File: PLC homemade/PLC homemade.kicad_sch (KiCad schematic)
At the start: 18 parts, among them J14 Conn_01x02, J15 Conn_01x02, U1 XC6220B331MR, U2 XL1509-5.0E1

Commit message: :ambulance:2output and usbc
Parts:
- J15: footprint Connector_PinHeader_1.00mm:PinHeader_1x02_P1.00mm_Vertical_SMD_Pin1Left -> PhoenixContact_GMSTBA_2,5_2-G_1x02_P7.50mm_Horizontal
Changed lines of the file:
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@@
 			)
 		)
-		(property "Footprint" "Connector_PinHeader_1.00mm:PinHeader_1x02_P1.00mm_Vertical_SMD_Pin1Left"
+		(property "Footprint" "PhoenixContact_GMSTBA_2,5_2-G_1x02_P7.50mm_Horizontal"
 			(at 105.41 72.39 0)
 			(effects

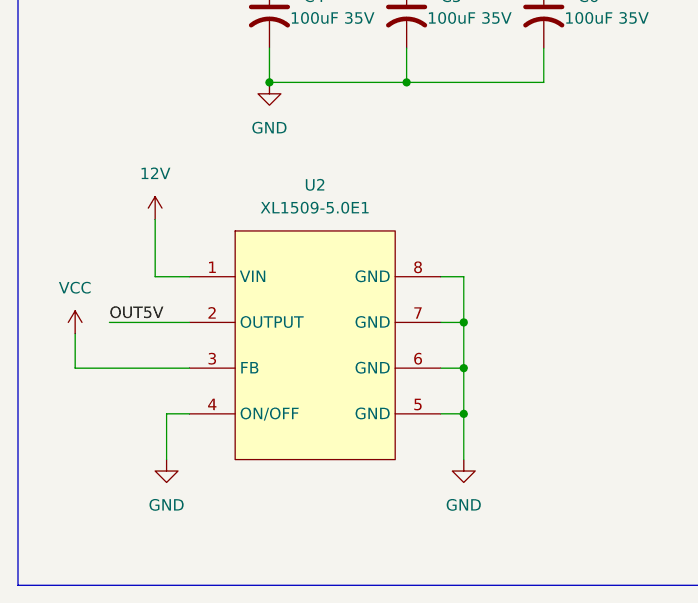
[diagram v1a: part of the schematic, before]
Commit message: :ambulance: Changed the 5 footprint error
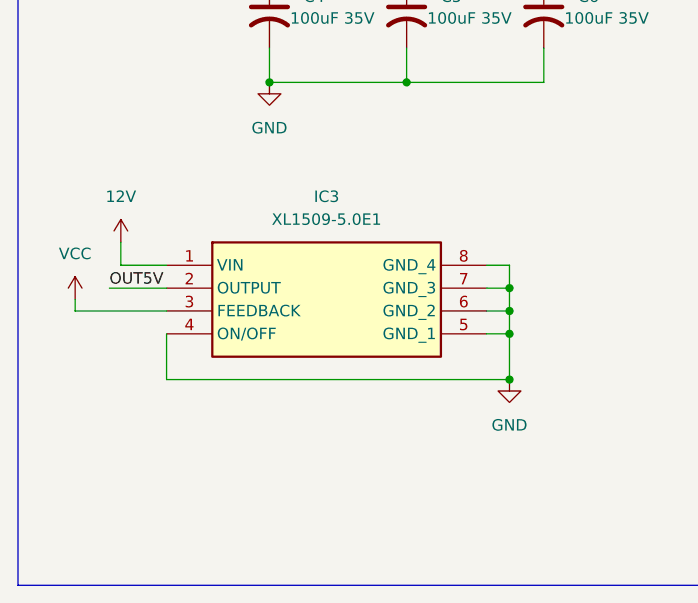
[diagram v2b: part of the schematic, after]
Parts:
- removed U2: XL1509-5.0E1, XL1509-5:SOIC-8_L5.0-W4.0-P1.27-LS6.0-BL, symbol XL1509-5.0E1:XL1509-5.0E1
- added IC3: XL1509-5.0E1, SOIC127P600X175-8N, symbol XL1509-5_0E1:XL1509-5.0E1
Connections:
- net 12V: now also IC3.1 (VIN)
- net GND: now also IC3.4 (ON/OFF), IC3.5 (GND_1), IC3.6 (GND_2), IC3.7 (GND_3), IC3.8 (GND_4)
- net OUT5V: now also IC3.2 (OUTPUT)
- net VCC: now also IC3.3 (FEEDBACK)
